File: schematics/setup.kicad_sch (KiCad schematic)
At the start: 1 part, among them U1 ESP32-S3-PICO-1-N8R2

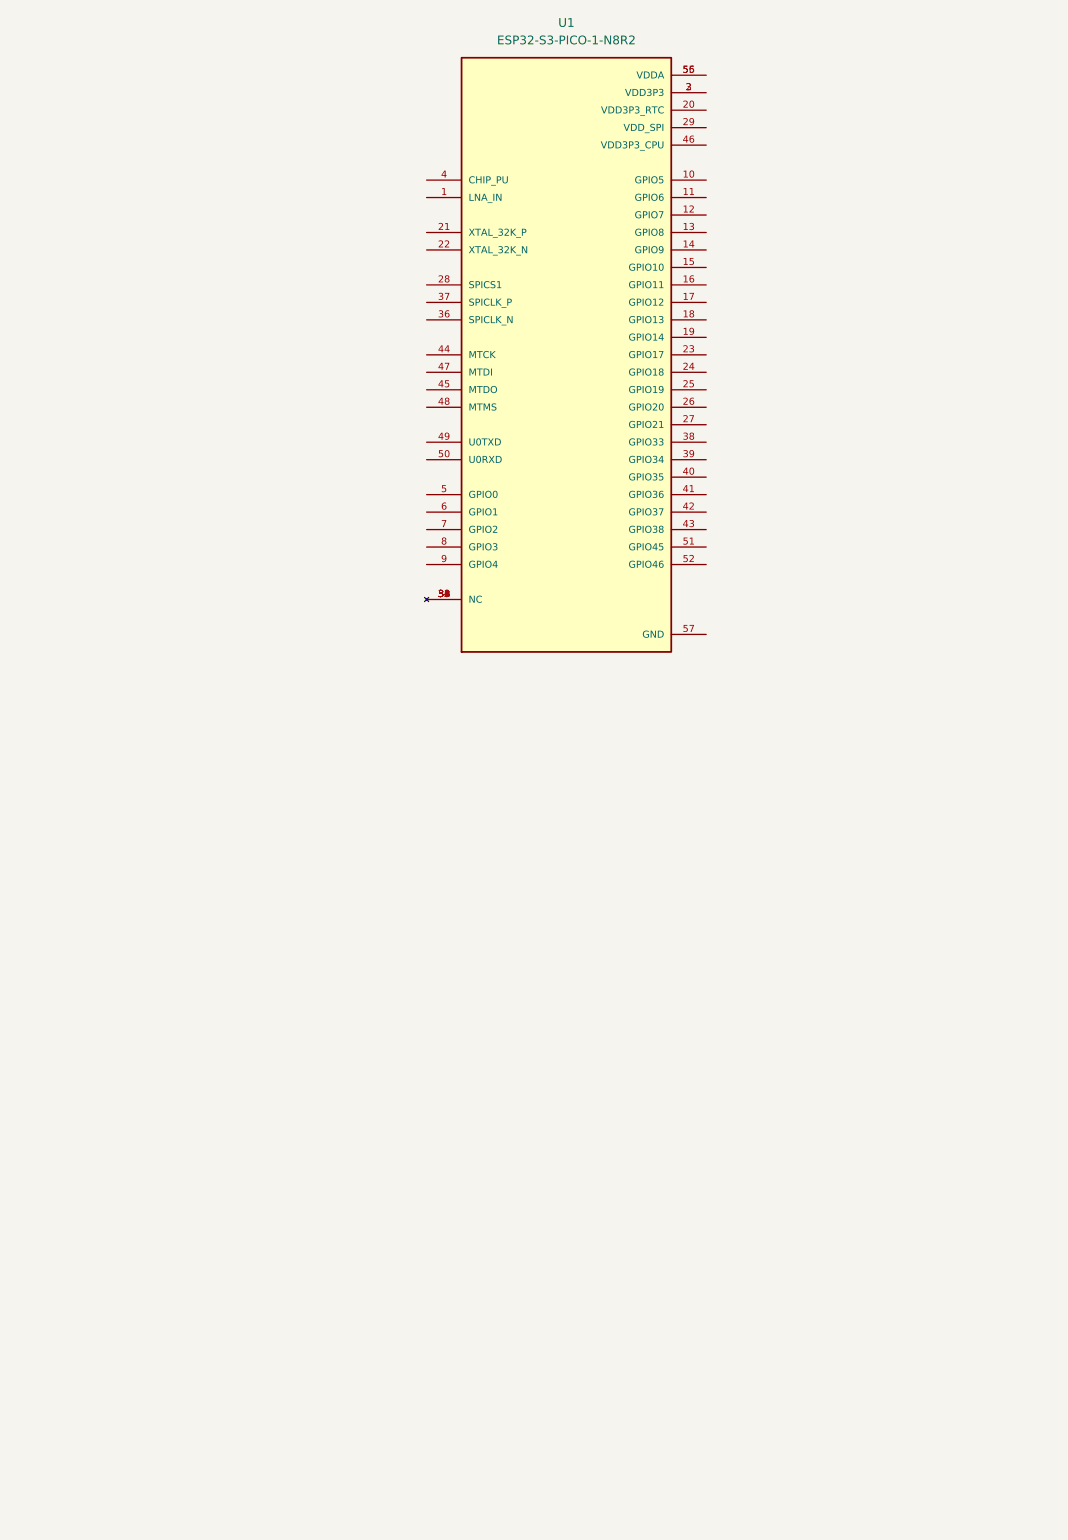
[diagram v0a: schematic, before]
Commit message: added init schematic
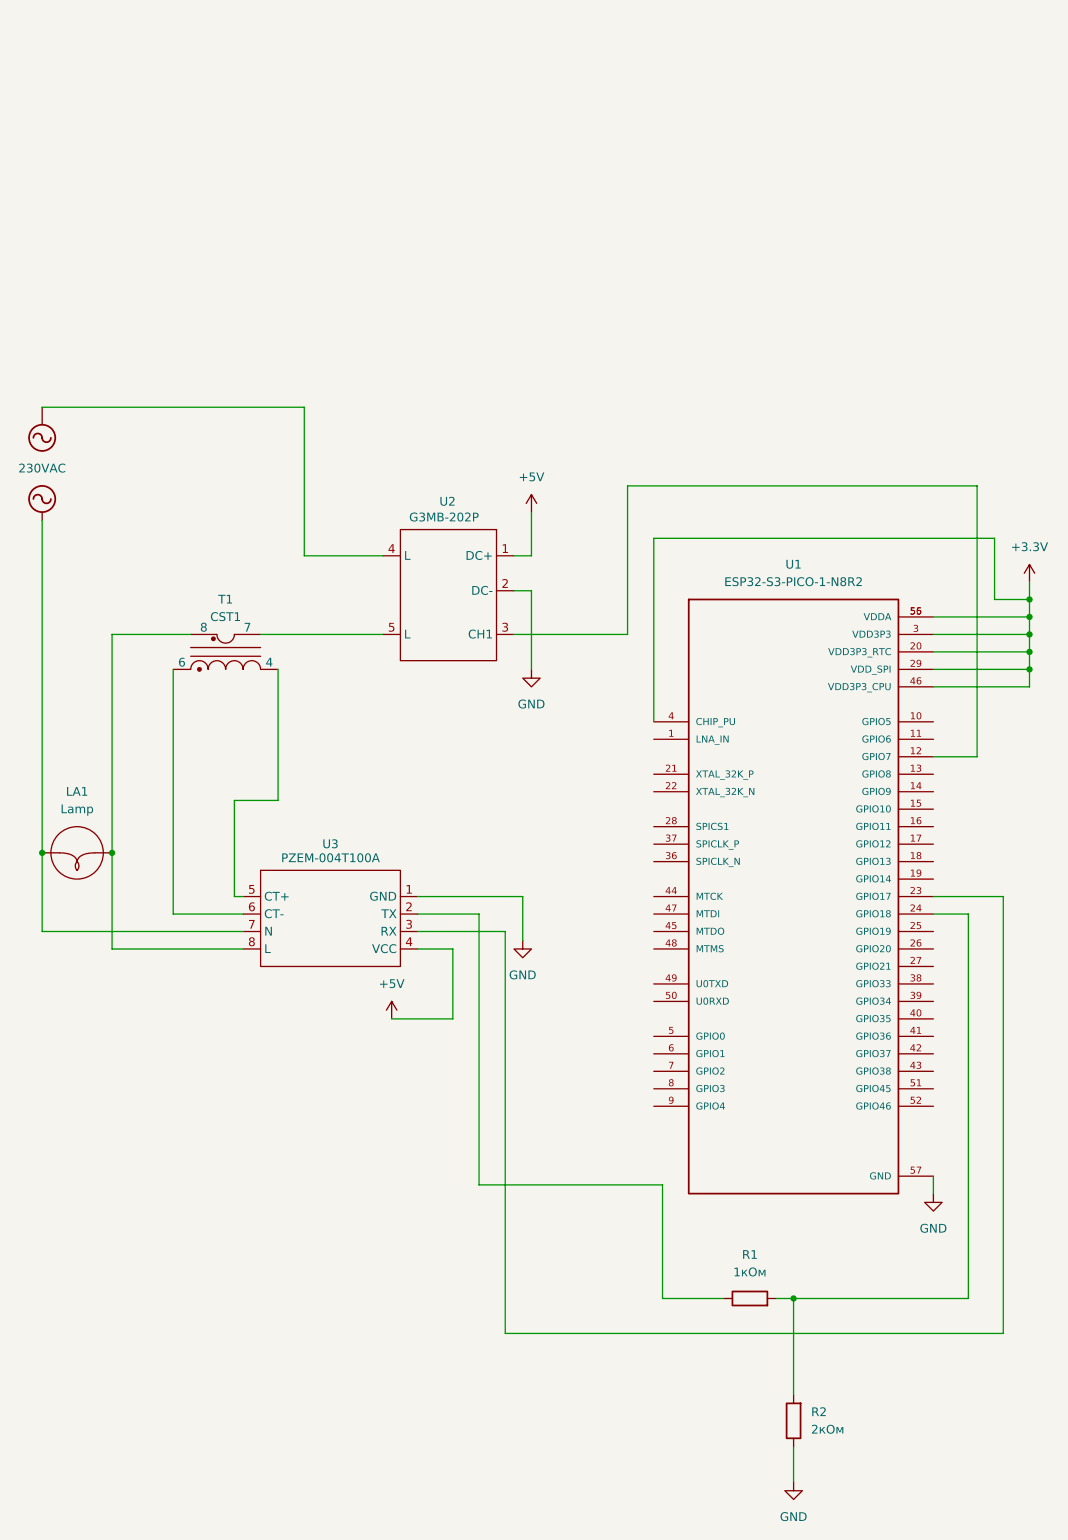
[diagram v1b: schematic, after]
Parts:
- added LA1: Lamp, symbol Device:Lamp
- added R1: 1кОм, symbol Device:R
- added R2: 2кОм, symbol Device:R
- added T1: CST1, Transformer_SMD:Transformer_Coilcraft_CST1, symbol Transformer:CST1
- added U2: G3MB-202P, G3MB-202P, symbol diploma:G3MB
- added U3: PZEM-004T100A, symbol diploma:PZEM004t
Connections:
- net at U1.12 (GPIO7): now also U2.3 (CH1)
- net +3.3V: now reaches U1.3 (VDD3P3)
- net +3.3V: now also U1.20 (VDD3P3_RTC), U1.29 (VDD_SPI), U1.4 (CHIP_PU), U1.46 (VDD3P3_CPU), U1.55 (VDDA), U1.56 (VDDA); no longer U1.2 (VDD3P3)
- net at U1.23 (GPIO17): now also U3.3 (RX)
- net at U1.24 (GPIO18): now also R1.2, R2.2
- net GND: now reaches U1.57 (GND)
- net GND: now also R2.1, U2.2 (DC-), U3.1 (GND)
- new net: T1.4, U3.5 (CT+)
- new net: T1.6, U3.6 (CT-)
- new net: T1.7, U2.5 (L)
- new net: LA1.2 (+), T1.8, U3.8 (L)
- new net: R1.1, U3.2 (TX)
- new net +5V: U2.1 (DC+), U3.4 (VCC)
- new net 230VAC: LA1.1 (-), U3.7 (N)
